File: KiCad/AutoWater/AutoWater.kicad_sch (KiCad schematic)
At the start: 46 parts, among them IC1 74ABT125PW, P1 Pump, Q1 Transistor NPN, SW1 Button, SW2 Button, Y1 32.768kHz

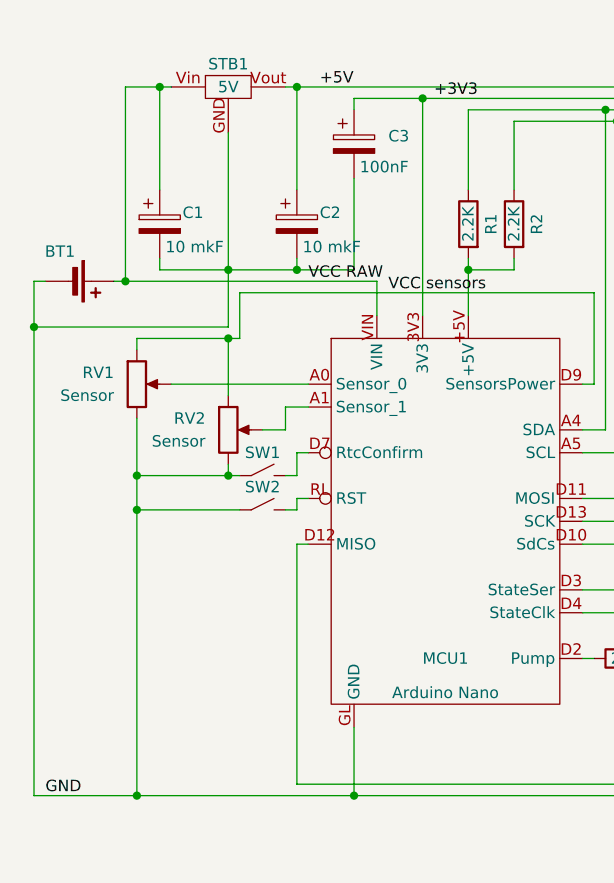
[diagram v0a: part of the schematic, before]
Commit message: Add power symbols
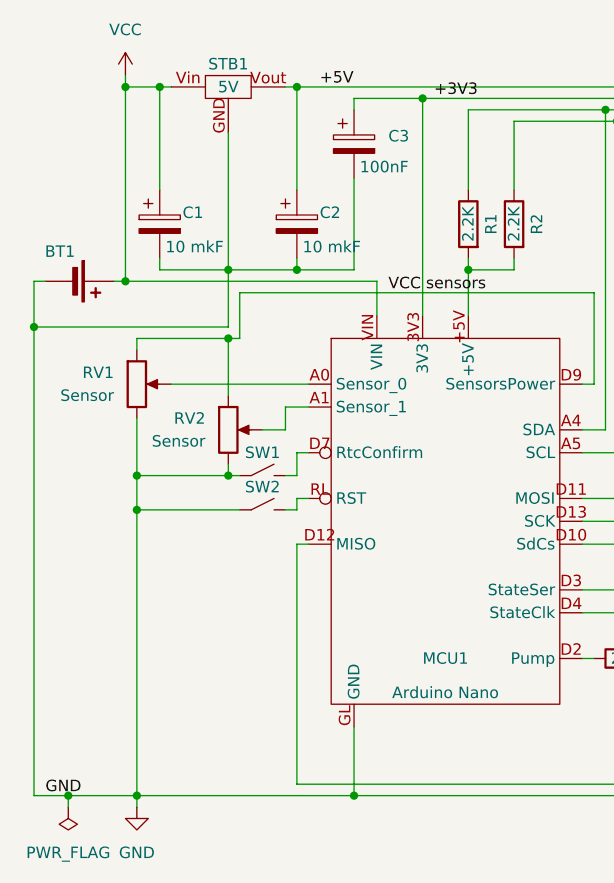
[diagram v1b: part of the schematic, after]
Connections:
- net VCC RAW renamed VCC
